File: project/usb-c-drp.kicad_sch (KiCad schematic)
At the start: 0 parts

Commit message: Added CubeMX project and some schematic components are added
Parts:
- added BT1: Battery_Cell, symbol Device:Battery_Cell
- added C78: 100p, symbol Device:C
- added C79: 10u, symbol Device:C
- added C80: 220u, bozi:GRM31_T30, symbol Device:C
- added C81: 2n2, bozi:GRM18_T10, symbol Device:C
- added C82: 100p, bozi:GRM15_T05, symbol Device:C
- added C83: 1u, bozi:GRM15_T05, symbol Device:C
- added C84: 4u7, bozi:GRM18_T15, symbol Device:C
- added C85: 100n, bozi:GRM18_T10, symbol Device:C
- added C86, C87: 470p, bozi:GRT15_T05, symbol Device:C
- added D2: TBD, symbol Device:D
- added D3: ESDA25P35-1U1M, ESDA25P351U1M, symbol bozi:ESDA25P35-1U1M
- added D4: LED, bozi:LEDC1608X70N_edit, symbol Device:LED
- added D5: BAT54KFILM, SODFL1608X70N, symbol bozi:BAT54KFILM
- added IC6, IC8: TCPP01-M12, QFN50P300X300X100-13N-D, symbol bozi:TCPP01-M12
- added IC7: ECMF02-2AMX6, SON50P150X170X55-6N-D, symbol bozi:ECMF02-2AMX6
- added Q1: STL11N3LLH6, STL20N6F7, symbol bozi:STL11N3LLH6
- added R10: 10K, bozi:RESC1005X37N_edit, symbol Device:R
- added R11, R12: 47K, bozi:RESC1005X37N_edit, symbol Device:R
- added R13: 2K4, bozi:RESC1005X37N_edit, symbol Device:R
- added R14, R15: 5K1, bozi:RESC1005X37N_edit, symbol Device:R
- added R8: 240, bozi:RESC1005X37N_edit, symbol Device:R
- added R9: 1, bozi:RESC1608X55N_edit, symbol Device:R
- added TP11: TestPoint, symbol Connector:TestPoint
- added TP12: TestPoint, TestPoint:TestPoint_Pad_D1.0mm, symbol Connector:TestPoint
- added U2: ~, symbol bozi:USB-C receptacle
- added U3: MCP73831-2-OT, Package_TO_SOT_SMD:SOT-23-5, symbol Battery_Management:MCP73831-2-OT
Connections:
- new net: C78.1, C79.1, D2.1 (K), TP11.1, U2.A4 (VBUS1), U2.A9 (VBUS2), U2.B4 (VBUS3), U2.B9 (VBUS4)
- new net: IC7.6 (D+), U2.A6 (D1+), U2.B6 (D2+)
- new net: IC7.5 (D-), U2.A7 (D1-), U2.B7 (D2-)
- new net: C84.2, R9.1
- new net: C81.1, C82.1, C83.1, D3.1 (K), D5.2 (A), Q1.5 (D), Q1.6 (D), Q1.7 (D), R10.1, R9.2
- new net: C81.2, IC8.5 (GATE), Q1.4 (G)
- new net: C85.2, D5.1 (K), IC8.8 (IN_GD)
- new net: D4.2 (A), R8.2
- new net: IC8.6 (VBUS_CTRL), R10.2, R13.1
- new net: IC8.1 (CC2), R12.2, R14.1
- new net: IC8.3 (CC1), R11.2, R15.1
- new net 5V_VIN: C80.1, IC8.4 (SOURCE), Q1.1 (S_1), Q1.2 (S_2), Q1.3 (S_3), R8.1, TP12.1
- new net GND: C78.2, C79.2, D2.2 (A), IC7.3 (GND), U2.A1 (GND1), U2.A12 (GND2), U2.B1 (GND3), U2.B12 (GND4), U2.SH1 (SHIELD1), U2.SH2 (SHIELD2), U2.SH3 (SHIELD3), U2.SH4 (SHIELD4)
- new net GNDREF: C80.2, C82.2, C83.2, C84.1, C85.1, C86.2, C87.2, D3.2 (A), D4.1 (K), IC8.13 (EP), IC8.2 (GND), R13.2, R14.2, R15.2
- new net USB_CC1: C86.1, IC8.7 (CC1C)
- new net USB_CC2: C87.1, IC8.9 (CC2C)
- new net USB_D_N: IC7.2 (D_2)
- new net USB_D_P: IC7.1 (D_1)
- new net USB_PWR_CC1: R11.1
- new net USB_PWR_CC2: R12.1
- new net VDD: IC8.10 (~{DB}), IC8.12 (VCC)
- no-connect marks 0 -> 12
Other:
- note added: ""GATE DRIVER""

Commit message: schemtic is done, need to go through BOM
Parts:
- removed C82: 100p, bozi:GRM15_T05, symbol Device:C
- removed C83: 1u, bozi:GRM15_T05, symbol Device:C
- removed D3: ESDA25P35-1U1M, ESDA25P351U1M, symbol bozi:ESDA25P35-1U1M
- removed D5: BAT54KFILM, SODFL1608X70N, symbol bozi:BAT54KFILM
- removed IC6: TCPP01-M12, QFN50P300X300X100-13N-D, symbol bozi:TCPP01-M12
- removed Q1: STL11N3LLH6, STL20N6F7, symbol bozi:STL11N3LLH6
- added C121: TBD, symbol Device:C
- added C85, C86: 4.7uF, symbol Device:C
- added D3: BAT54KFILM, bozi:SODFL1608X70N_edit, symbol Device:D
- added D5: LED, bozi:LEDC1608X70N_edit, symbol Device:LED
- added IC12: MAX17262REWL+T, BGA9C40P3X3_147X145X69, symbol bozi:MAX17262REWL+T
- added IC6: TPS2117DRLR, SOTFL50P160X60-8N, symbol bozi:TPS2117DRLR
- added Q2: STL11N3LLH6, bozi:STL20N6F7_edit, symbol Transistor_FET:Q_NMOS_DGS
- added R31: TBD (configuration resistor), symbol Device:R
- added R32: TBD (based on color on LED), symbol Device:R
- added R33, R34: TBD, symbol Device:R
- added R71, R72, R73, R74, R75, R76, R77, R78, R79: 0R, bozi:RESC1005X37N_edit, symbol Device:R
- added TH1: 10K NTC, bozi:THRMC1005X55N, symbol Device:Thermistor_NTC
- BT1: Manufacturer_Name (none) -> x; Manufacturer_Part_Number (none) -> x
- C81: renamed from C78; value 100p -> 100pF; Manufacturer_Name (none) -> Murata Electronics; Manufacturer_Part_Number (none) -> GRM0335C1H101JA01D
- C82: renamed from C79; value 10u -> 1uF; footprint (none) -> bozi:GRM15_T05; Manufacturer_Name (none) -> Murata Electronics; Manufacturer_Part_Number (none) -> GRM155R61E105KA12D
- C83: renamed from C80; value 220u -> 220uF; Manufacturer_Name (none) -> Murata Electronics
- C84: renamed from C81; value 2n2 -> 2.2uF; Manufacturer_Name (none) -> Murata Electronics
- C87: renamed from C84; value 4u7 -> 4.7uF; Manufacturer_Name (none) -> Murata Electronics
- C88: renamed from C85; value 100n -> 100nF; Manufacturer_Name (none) -> Murata Electronics
- C89: renamed from C86; value 470p -> 470pF; Manufacturer_Name (none) -> Murata Electronics
- C90: renamed from C87; value 470p -> 470pF; Manufacturer_Name (none) -> Murata Electronics
- D2: value TBD -> TVS / TBD
- D4: Manufacturer_Name (none) -> Würth Elektronik
- R12: renamed from R8; value 240 -> 240R; Manufacturer_Name (none) -> YAGEO
- R13: renamed from R9; value 1 -> 1R; Manufacturer_Name (none) -> Yageo
- R14: renamed from R10; Manufacturer_Name (none) -> YAGEO
- R15: renamed from R11; Manufacturer_Name (none) -> YAGEO
- R16: renamed from R12; Manufacturer_Name (none) -> YAGEO
- R17: renamed from R13; value 2K4 -> 2.4K; Manufacturer_Name (none) -> YAGEO
- R18: renamed from R14; value 5K1 -> 5.1K; Manufacturer_Name (none) -> YAGEO
- R19: renamed from R15; value 5K1 -> 5.1K; Manufacturer_Name (none) -> YAGEO
- U2: value ~ -> USB C DRP; footprint (none) -> bozi:2012670005_edit; Manufacturer_Name (none) -> Molex; Manufacturer_Part_Number (none) -> 2012670005
- U3: symbol Battery_Management:MCP73831-2-OT -> bozi:MCP73831-2-OT; Manufacturer_Name (none) -> Microchip Technology; Manufacturer_Part_Number (none) -> MCP73831-2ATI/MC-ND
- renumbered TP11 to TP16, TP12 to TP17
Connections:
- net 5V_VIN: now also Q2.3 (S), R72.1, R75.1
- net GND: now also BT1.2 (-), U3.2 (V_{SS}), C121.2, C85.2, C86.2, IC12.C3 (GND), R31.2, TH1.2
- net GNDREF: now also IC6.1 (GND), R34.2
- net USB_CC1: now also U2.A5 (CC1)
- net USB_CC2: now also U2.B5 (CC2)
- net at C81.1, C82.1, D2.1 (K)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: now also C84.2, R13.2, R14.1, D3.2 (A), Q2.1 (D)
- net at IC8.5 (GATE): now also C84.1, Q2.2 (G); no longer C84.2
- net at C88.2, IC8.8 (IN_GD): now also D3.1 (K)
- net at BT1.1 (+): now also U3.3 (V_{BAT}), C85.1, R71.1, R74.1
- net at U3.1 (STAT): now also R32.2
- net at U3.4 (V_{DD}): now also C86.1, D5.2 (A), R72.2
- net at U3.5 (PROG): now also R31.1
- new net: IC6.3 (VIN1), IC6.5 (MODE), R33.1, R76.2, R78.1
- new net: IC12.B3 (SYS), R73.1
- new net: IC6.4 (PR1), R33.2, R34.1
- new net: C121.1, IC12.C2 (REG)
- new net: IC6.2 (VOUT_1), IC6.7 (VOUT_2), R77.2
- new net: IC6.6 (VIN2), R75.2, R79.1
- new net: D5.1 (K), R32.1
- new net: IC12.A2 (BATT), R74.2
- new net: IC12.A1 (TH), TH1.1
- new net BFG_ALRT: IC12.B2 (ALRT)
- new net BFG_SCL: IC12.B1 (SCL)
- new net BFG_SDA: IC12.C1 (SDA)
- new net VBAT: R71.2, R73.2, R76.1
- new net VSOURCE_IO: IC6.8 (ST)
- new net VSYS: R77.1, R78.2, R79.2
- no-connect marks 12 -> 13
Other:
- note added: "Battery charger"
- note added: "Battery fuel gauge"
- note added: "Double check logic"
- note added: "Voltage source selection logic: 5V_VIN has priority over VBAT"
- note added: "When VBAT is less than 3.75, then VOUT is equal to 5V_VIN"
- moved on the sheet: BT1, C81, C82, C84, C87, C89, C90, D2, IC7, IC8, R13, TP16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

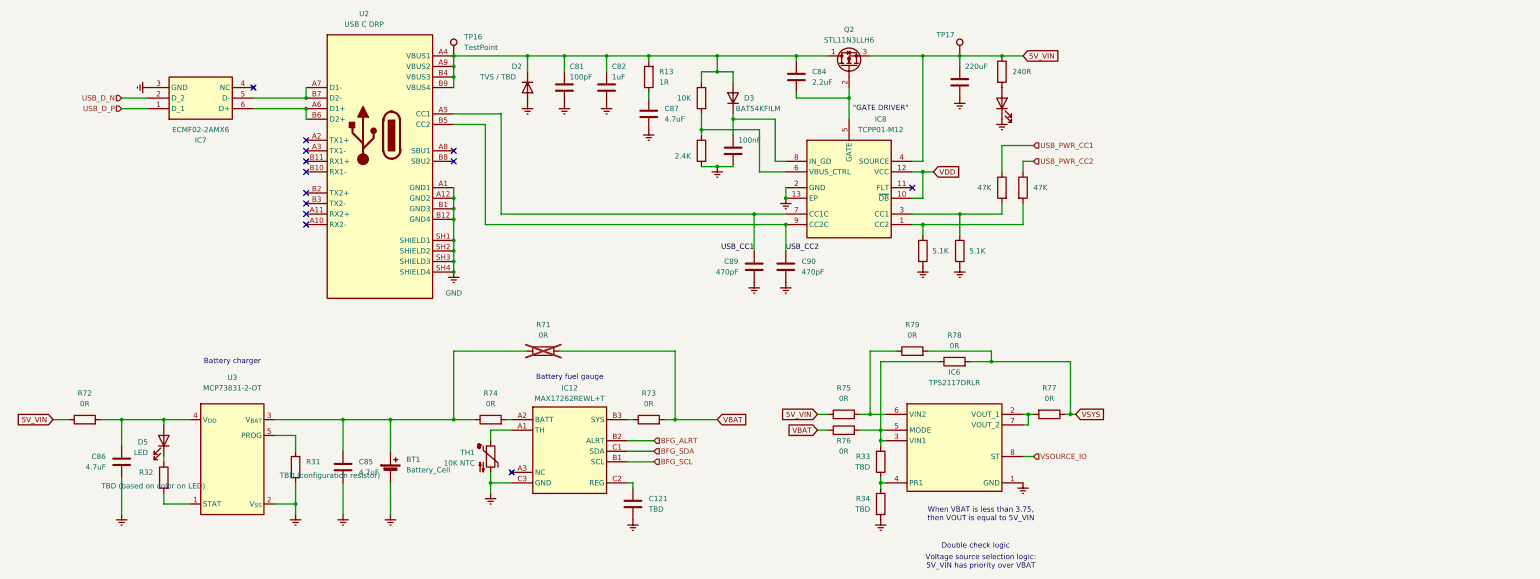
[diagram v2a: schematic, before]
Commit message: schemtic is done, annotation set
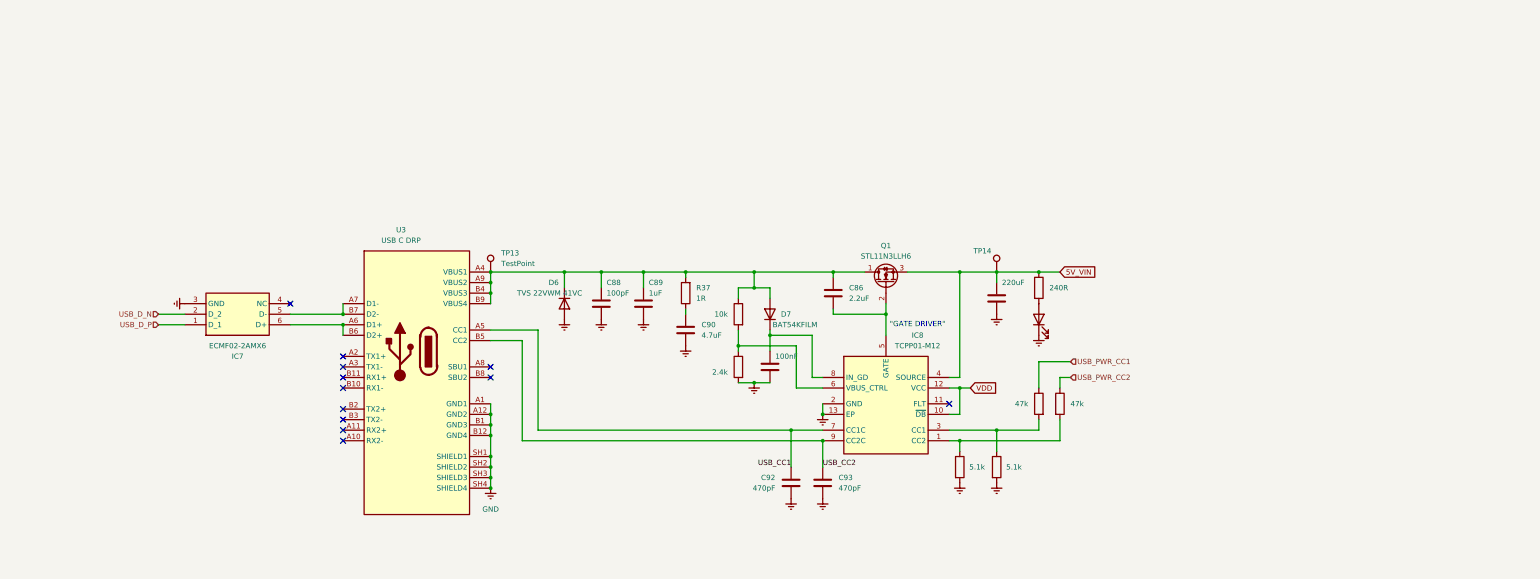
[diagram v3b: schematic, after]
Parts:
- removed BT1: Battery_Cell, symbol Device:Battery_Cell
- removed C121: TBD, symbol Device:C
- removed C85, C86: 4.7uF, symbol Device:C
- removed D5: LED, bozi:LEDC1608X70N_edit, symbol Device:LED
- removed IC12: MAX17262REWL+T, BGA9C40P3X3_147X145X69, symbol bozi:MAX17262REWL+T
- removed IC6: TPS2117DRLR, SOTFL50P160X60-8N, symbol bozi:TPS2117DRLR
- removed R31: TBD (configuration resistor), symbol Device:R
- removed R32: TBD (based on color on LED), symbol Device:R
- removed R33, R34: TBD, symbol Device:R
- removed R71, R72, R73, R74, R75, R76, R77, R78, R79: 0R, bozi:RESC1005X37N_edit, symbol Device:R
- removed TH1: 10K NTC, bozi:THRMC1005X55N, symbol Device:Thermistor_NTC
- removed U3: MCP73831-2-OT, Package_TO_SOT_SMD:SOT-23-5, symbol bozi:MCP73831-2-OT
- C88: renamed from C81; footprint (none) -> bozi:GRM03T09
- D6: renamed from D2; value TVS / TBD -> TVS 22VWM 41VC; footprint (none) -> bozi:ESDA25P351U1M_edit; Manufacturer_Name (none) -> STMicroelectronics; Manufacturer_Part_Number (none) -> ESDA25P35-1U1M
- R38: renamed from R14; value 10K -> 10k
- R39: renamed from R17; value 2.4K -> 2.4k
- R40: renamed from R15; value 47K -> 47k
- R41: renamed from R16; value 47K -> 47k
- R42: renamed from R18; value 5.1K -> 5.1k
- R43: renamed from R19; value 5.1K -> 5.1k
- renumbered C84 to C86, C83 to C87, C82 to C89, C87 to C90, C88 to C91, C89 to C92, C90 to C93, D3 to D7, D4 to D8, Q2 to Q1, R12 to R36, R13 to R37, TP16 to TP13, TP17 to TP14, U2 to U3
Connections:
- no-connect marks 13 -> 12
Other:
- note removed: "Battery charger"
- note removed: "Battery fuel gauge"
- note removed: "Double check logic"
- note removed: "Voltage source selection logic: 5V_VIN has priority over VBAT"
- note removed: "When VBAT is less than 3.75, then VOUT is equal to 5V_VIN"
- moved on the sheet: C86, C88, C89, C90, C92, C93, D6, D7, IC7, IC8, Q1, R37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

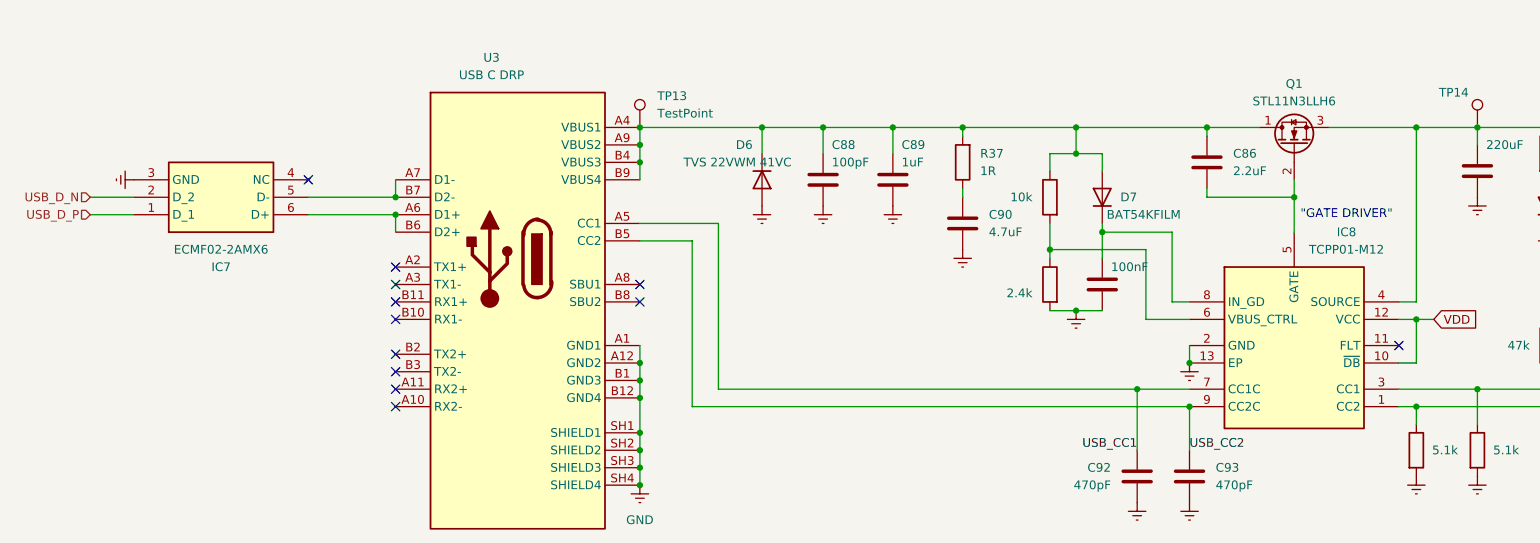
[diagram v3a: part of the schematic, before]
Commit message: PCB design, finished RAM, audio, battery fuel gauge and charger, PMIC, USB C power
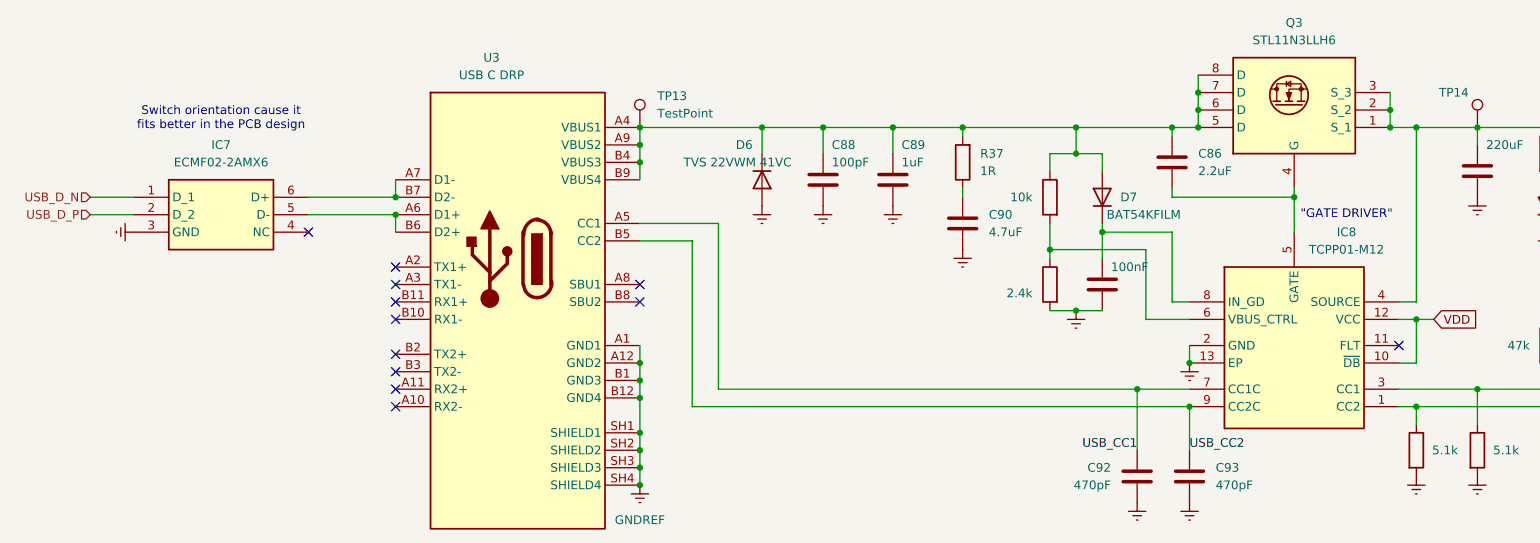
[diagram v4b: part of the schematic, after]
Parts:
- removed Q1: STL11N3LLH6, bozi:STL20N6F7_edit, symbol Transistor_FET:Q_NMOS_DGS
- added Q3: STL11N3LLH6, bozi:STL20N6F7_edit, symbol bozi:STL11N3LLH6
- C88: footprint bozi:GRM03T09 -> bozi:GRM03_T09
- IC7: footprint SON50P150X170X55-6N-D -> bozi:SON50P150X170X55-6N-D_edit
- IC8: footprint QFN50P300X300X100-13N-D -> bozi:QFN50P300X300X100-13N-D_edit
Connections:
- net 5V_VIN: now also Q3.1 (S_1), Q3.2 (S_2), Q3.3 (S_3)
- net GND: no longer U3.A1 (GND1), U3.A12 (GND2), U3.B1 (GND3), U3.B12 (GND4), U3.SH1 (SHIELD1), U3.SH2 (SHIELD2), U3.SH3 (SHIELD3), U3.SH4 (SHIELD4)
- net GNDREF: now also U3.A1 (GND1), U3.A12 (GND2), U3.B1 (GND3), U3.B12 (GND4), U3.SH1 (SHIELD1), U3.SH2 (SHIELD2), U3.SH3 (SHIELD3), U3.SH4 (SHIELD4)
- net USB_D_N: now also IC7.1 (D_1); no longer IC7.2 (D_2)
- net USB_D_P: now also IC7.2 (D_2); no longer IC7.1 (D_1)
- net at C86.2, C88.1, C89.1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: now also Q3.5 (D), Q3.6 (D), Q3.7 (D), Q3.8 (D)
- net at U3.A6 (D1+), U3.B6 (D2+): now also IC7.5 (D-); no longer IC7.6 (D+)
- net at U3.A7 (D1-), U3.B7 (D2-): now also IC7.6 (D+); no longer IC7.5 (D-)
- net at C86.1, IC8.5 (GATE): now also Q3.4 (G)
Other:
- note added: "Switch orientation cause it fits better in the PCB design"
- moved on the sheet: C86, IC7
